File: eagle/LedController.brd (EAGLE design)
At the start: 64.8 x 34.3 mm, 21 parts, among them IC2 MEGA8-P, IC3 7805, Q1 16MHz, Q2 FDS8884, Q3 FDS8884, Q4 FDS8884, Q5 FDS8884, X1 2510-, X2 MKDSN1,5/4-5,08

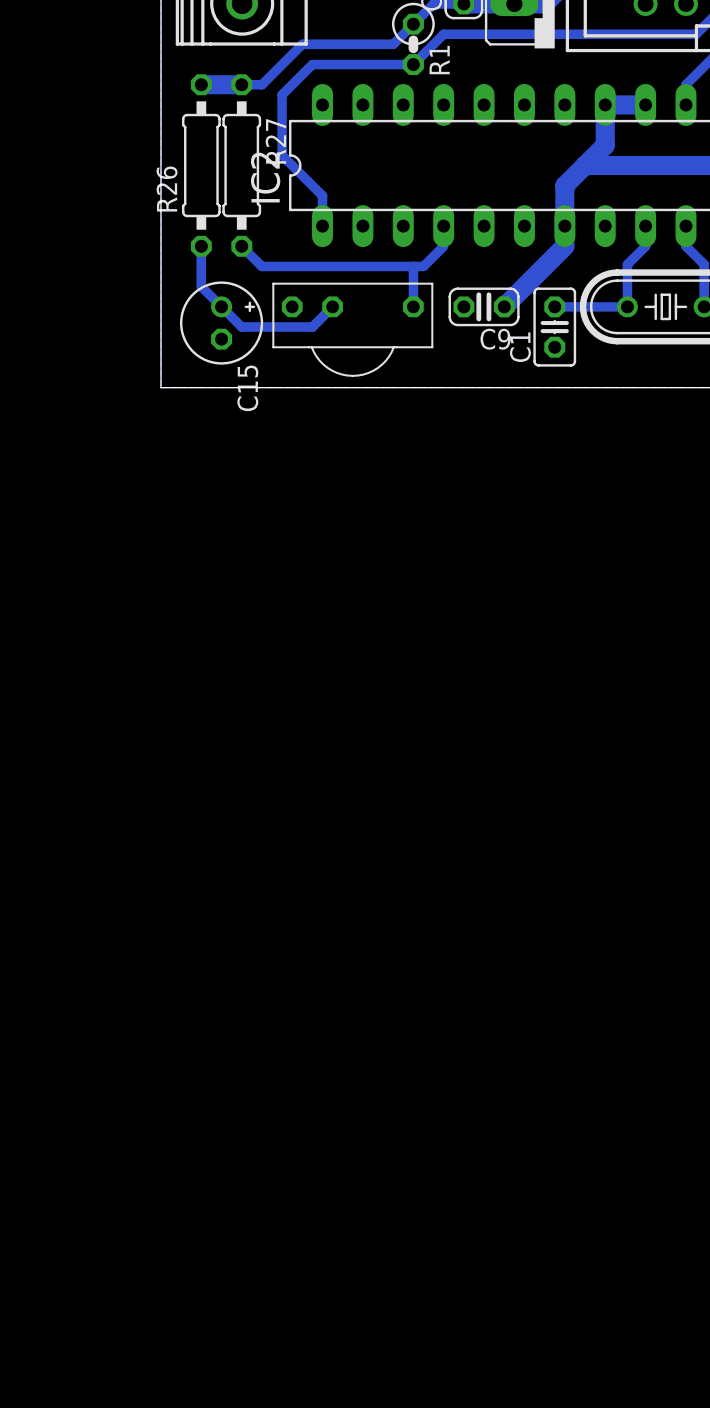
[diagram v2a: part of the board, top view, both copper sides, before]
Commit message: add preamp stage for microphone
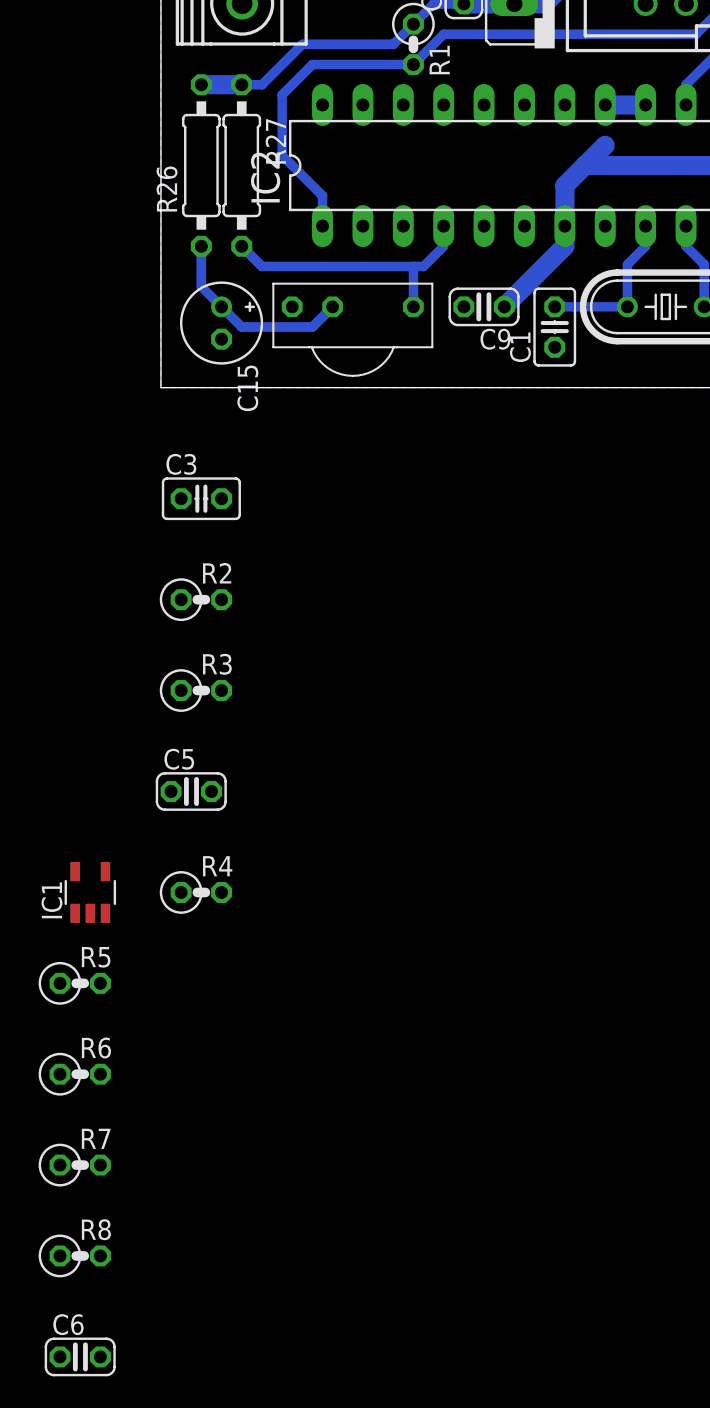
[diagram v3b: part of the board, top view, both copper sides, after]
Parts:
- added C3: 100nF, rcl:C025-025X050
- added C5: 1uF, rcl:C025-024X044
- added C6: 4n7, rcl:C025-024X044
- added IC1: MCP601R, linear:SOT23-5
- added R2: 100, rcl:0207/2V
- added R3, R4: 1k, rcl:0207/2V
- added R5, R6, R7: 10k, rcl:0207/2V
- added R8: 12k, rcl:0207/2V
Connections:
- new net ADC: C6.2, IC2.23, R8.2
- new net N$1: C5.1, R3.1
- new net N$10: IC1.4, R4.1
- new net N$11: IC1.3, R5.2, R6.1
- new net N$12: IC1.1, R7.2, R8.1
- new net N$7: C3.1, IC2.20, IC2.21, R2.1
- new net N$9: C5.2, R4.2, R7.1
- net +5V: now also IC1.2, R2.2, R3.2, R5.1; no longer IC2.20, IC2.21
- net GND: now also C3.2, C6.1, IC1.5, R6.2
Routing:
- net +5V: track 98.4 -> 93.3 mm
- net N$7: track 0.00 -> 2.54 mm
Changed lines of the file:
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@@
 <element name="R1" library="rcl" package="0207/2V" value="10k" x="15.875" y="21.59" rot="R270"/>
 <element name="Q5" library="FDS8884" package="SO08" value="FDS8884" x="12.065" y="28.575" rot="MR180"/>
+<element name="C3" library="rcl" package="C025-025X050" value="100nF" x="2.54" y="-6.985"/>
+<element name="R2" library="rcl" package="0207/2V" value="100" x="2.54" y="-13.335"/>
+<element name="R3" library="rcl" package="0207/2V" value="1k" x="2.54" y="-19.05"/>
+<element name="C5" library="rcl" package="C025-024X044" value="1uF" x="1.905" y="-25.4"/>
+<element name="R4" library="rcl" package="0207/2V" value="1k" x="2.54" y="-31.75"/>
+<element name="IC1" library="linear" package="SOT23-5" value="MCP601R" x="-4.445" y="-31.75"/>
+<element name="R5" library="rcl" package="0207/2V" value="10k" x="-5.08" y="-37.465"/>
+<element name="R6" library="rcl" package="0207/2V" value="10k" x="-5.08" y="-43.18"/>
+<element name="R7" library="rcl" package="0207/2V" value="10k" x="-5.08" y="-48.895"/>
+<element name="R8" library="rcl" package="0207/2V" value="12k" x="-5.08" y="-54.61"/>
+<element name="C6" library="rcl" package="C025-024X044" value="4n7" x="-5.08" y="-60.96"/>
 </elements>
 <signals>
@@
 <contactref element="Q5" pad="2"/>
 <contactref element="Q5" pad="3"/>
+<contactref element="C3" pad="2"/>
+<contactref element="R6" pad="2"/>
+<contactref element="IC1" pad="5"/>
+<contactref element="C6" pad="1"/>
+<wire x1="38.1" y1="26.67" x2="40.64" y2="26.67" width="0" layer="19" extent="1-1"/>
+<wire x1="35.56" y1="26.67" x2="38.1" y2="26.67" width="0" layer="19" extent="1-1"/>
+<wire x1="33.02" y1="26.67" x2="35.56" y2="26.67" width="0" layer="19" extent="1-1"/>
+<wire x1="22.225" y1="26.67" x2="33.02" y2="26.67" width="0" layer="19" extent="1-1"/>
+<wire x1="19.05" y1="26.67" x2="22.225" y2="26.67" width="0" layer="19" extent="1-1"/>
+<wire x1="16.51" y1="26.67" x2="19.05" y2="26.67" width="0" layer="19" extent="1-1"/>
+<wire x1="16.764" y1="31.75" x2="16.51" y2="26.67" width="0" layer="19" extent="1-1"/>
+<wire x1="12.7" y1="31.6484" x2="16.764" y2="31.75" width="0" layer="19" extent="16-16"/>
+<wire x1="11.43" y1="31.6484" x2="12.7" y2="31.6484" width="0" layer="19" extent="16-16"/>
+<wire x1="10.16" y1="31.6484" x2="11.43" y2="31.6484" width="0" layer="19" extent="16-16"/>
+<wire x1="25.4" y1="17.78" x2="22.225" y2="26.67" width="0" layer="19" extent="1-1"/>
+<wire x1="27.94" y1="10.16" x2="25.4" y2="17.78" width="0" layer="19" extent="1-1"/>
+<wire x1="24.765" y1="2.54" x2="27.94" y2="10.16" width="0" layer="19" extent="1-1"/>
+<wire x1="19.05" y1="5.08" x2="24.765" y2="2.54" width="0" layer="19" extent="1-1"/>
+<wire x1="8.255" y1="5.08" x2="19.05" y2="5.08" width="0" layer="19" extent="1-1"/>
+<wire x1="3.81" y1="3.048" x2="8.255" y2="5.08" width="0" layer="19" extent="1-1"/>
+<wire x1="3.81" y1="-6.985" x2="3.81" y2="3.048" width="0" layer="19" extent="1-1"/>
+<wire x1="38.735" y1="2.54" x2="27.94" y2="10.16" width="0" layer="19" extent="1-1"/>
+<wire x1="50.2666" y1="3.175" x2="38.735" y2="2.54" width="0" layer="19" extent="16-16"/>
+<wire x1="50.2666" y1="4.445" x2="50.2666" y2="3.175" width="0" layer="19" extent="16-16"/>
+<wire x1="50.2666" y1="1.905" x2="50.2666" y2="3.175" width="0" layer="19" extent="16-16"/>
+<wire x1="50.2666" y1="8.255" x2="50.2666" y2="4.445" width="0" layer="19" extent="16-16"/>
+<wire x1="50.2666" y1="9.525" x2="50.2666" y2="8.255" width="0" layer="19" extent="16-16"/>
+<wire x1="50.2666" y1="10.795" x2="50.2666" y2="9.525" width="0" layer="19" extent="16-16"/>
+<wire x1="50.2666" y1="14.605" x2="50.2666" y2="10.795" width="0" layer="19" extent="16-16"/>
+<wire x1="50.2666" y1="15.875" x2="50.2666" y2="14.605" width="0" layer="19" extent="16-16"/>
+<wire x1="50.2666" y1="17.145" x2="50.2666" y2="15.875" width="0" layer="19" extent="16-16"/>
+<wire x1="-5.395" y1="-30.444" x2="3.81" y2="-6.985" width="0" layer="19" extent="1-1"/>
+<wire x1="-3.81" y1="-43.18" x2="-5.395" y2="-30.444" width="0" layer="19" extent="1-1"/>
+<wire x1="-6.35" y1="-60.96" x2="-3.81" y2="-43.18" width="0" layer="19" extent="1-1"/>
 </signal>
 <signal name="N$2">
@@
 <contactref element="IC2" pad="7"/>
 <contactref element="R1" pad="1"/>
-<contactref element="IC2" pad="21"/>
-<contactref element="IC2" pad="20"/>
 <contactref element="R27" pad="1"/>
 <contactref element="R26" pad="2"/>
@@
 <wire x1="25.4" y1="12.7" x2="26.67" y2="13.97" width="1.2" layer="16"/>
 <wire x1="26.67" y1="13.97" x2="27.94" y2="15.24" width="1.2" layer="16"/>
-<wire x1="27.94" y1="15.24" x2="27.94" y2="17.78" width="1.2" layer="16"/>
 <wire x1="22.225" y1="24.13" x2="24.13" y2="24.13" width="1.2" layer="16"/>
 <wire x1="24.13" y1="24.13" x2="29.21" y2="29.21" width="1.2" layer="16"/>
@@
 <wire x1="43.18" y1="13.97" x2="26.67" y2="13.97" width="1.2" layer="16"/>
 <wire x1="30.48" y1="26.67" x2="30.48" y2="29.21" width="1.2" layer="16"/>
-<wire x1="27.94" y1="17.78" x2="30.48" y2="17.78" width="1.2" layer="16"/>
 <wire x1="2.54" y1="19.05" x2="5.08" y2="19.05" width="1.2" layer="16"/>
 <wire x1="19.05" y1="24.13" x2="22.225" y2="24.13" width="1.2" layer="16"/>
@@
 <wire x1="15.875" y1="22.86" x2="17.145" y2="24.13" width="0.6" layer="16"/>
 <wire x1="17.145" y1="24.13" x2="19.05" y2="24.13" width="0.6" layer="16"/>
+<contactref element="R2" pad="2"/>
+<contactref element="R3" pad="2"/>
+<contactref element="R5" pad="1"/>
+<contactref element="IC1" pad="2"/>
+<wire x1="-4.445" y1="-33.056" x2="-6.35" y2="-37.465" width="0" layer="19" extent="1-1"/>
+<wire x1="3.81" y1="-19.05" x2="-4.445" y2="-33.056" width="0" layer="19" extent="1-1"/>
+<wire x1="3.81" y1="-13.335" x2="3.81" y2="-19.05" width="0" layer="19" extent="1-1"/>
+<wire x1="21.59" y1="5.08" x2="3.81" y2="-13.335" width="0" layer="19" extent="1-1"/>
 </signal>
 <signal name="ISP_RESET">
@@
 <wire x1="38.1" y1="8.89" x2="38.1" y2="10.16" width="0.6" layer="16"/>
 </signal>
+<signal name="ADC">
+<contactref element="IC2" pad="23"/>
+<contactref element="R8" pad="2"/>
+<contactref element="C6" pad="2"/>
+<wire x1="-3.81" y1="-54.61" x2="-3.81" y2="-60.96" width="0" layer="19" extent="1-1"/>
+<wire x1="22.86" y1="17.78" x2="-3.81" y2="-54.61" width="0" layer="19" extent="1-1"/>
+</signal>
+<signal name="N$7">
+<contactref element="IC2" pad="21"/>
+<contactref element="IC2" pad="20"/>
+<wire x1="27.94" y1="17.78" x2="30.48" y2="17.78" width="1.2" layer="16"/>
+<contactref element="R2" pad="1"/>
+<contactref element="C3" pad="1"/>
+<wire x1="1.27" y1="-6.985" x2="27.94" y2="17.78" width="0" layer="19" extent="1-1"/>
+<wire x1="1.27" y1="-13.335" x2="1.27" y2="-6.985" width="0" layer="19" extent="1-1"/>
+</signal>
+<signal name="N$1">
+<contactref element="R3" pad="1"/>
+<contactref element="C5" pad="1"/>
+<wire x1="1.27" y1="-19.05" x2="0.635" y2="-25.4" width="0" layer="19" extent="1-1"/>
+</signal>
+<signal name="N$9">
+<contactref element="C5" pad="2"/>
+<contactref element="R4" pad="2"/>
+<contactref element="R7" pad="1"/>
+<wire x1="3.81" y1="-31.75" x2="-6.35" y2="-48.895" width="0" layer="19" extent="1-1"/>
+<wire x1="3.175" y1="-25.4" x2="3.81" y2="-31.75" width="0" layer="19" extent="1-1"/>
+</signal>
+<signal name="N$10">
+<contactref element="R4" pad="1"/>
+<contactref element="IC1" pad="4"/>
+<wire x1="-3.495" y1="-30.444" x2="1.27" y2="-31.75" width="0" layer="19" extent="1-1"/>
+</signal>
+<signal name="N$11">
+<contactref element="R5" pad="2"/>
+<contactref element="R6" pad="1"/>
+<contactref element="IC1" pad="3"/>
+<wire x1="-3.81" y1="-37.465" x2="-6.35" y2="-43.18" width="0" layer="19" extent="1-1"/>
+<wire x1="-3.495" y1="-33.056" x2="-3.81" y2="-37.465" width="0" layer="19" extent="1-1"/>
+</signal>
+<signal name="N$12">
+<contactref element="R7" pad="2"/>
+<contactref element="IC1" pad="1"/>
+<contactref element="R8" pad="1"/>
+<wire x1="-3.81" y1="-48.895" x2="-6.35" y2="-54.61" width="0" layer="19" extent="1-1"/>
+<wire x1="-5.395" y1="-33.056" x2="-3.81" y2="-48.895" width="0" layer="19" extent="1-1"/>
+</signal>
 </signals>

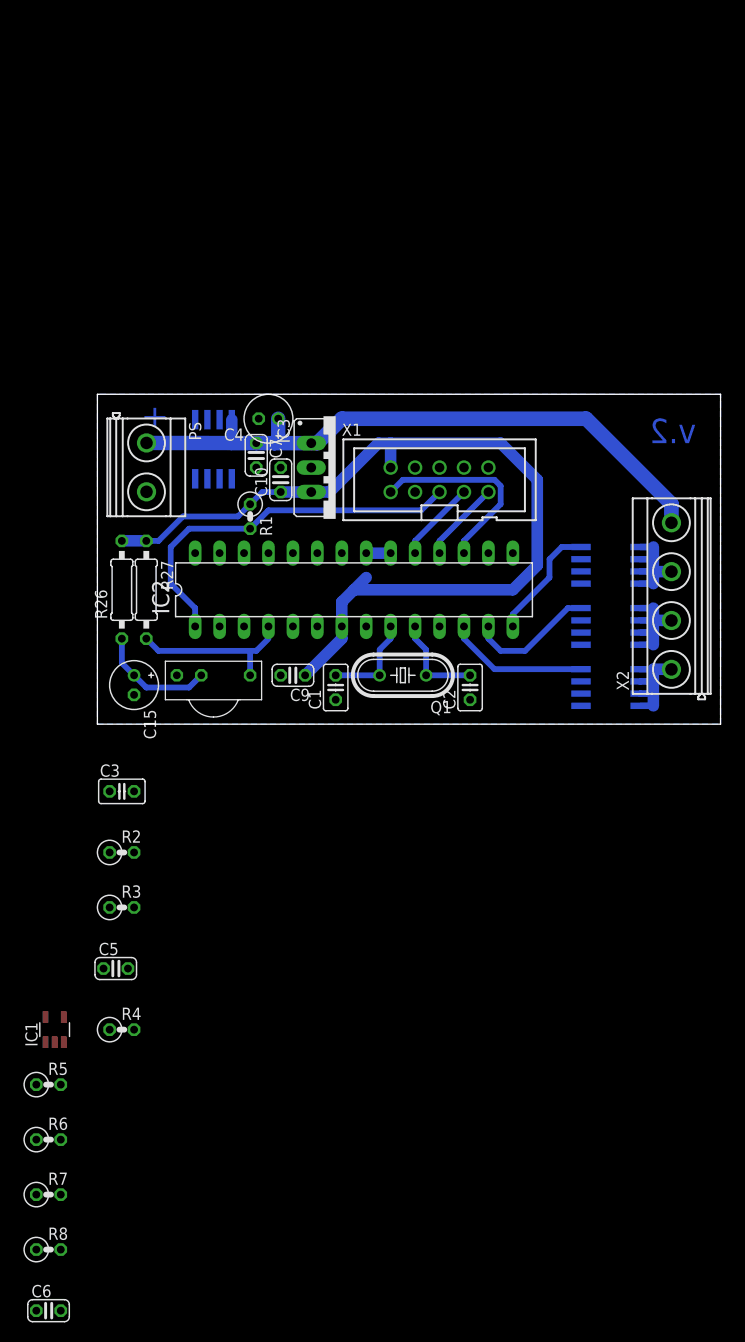
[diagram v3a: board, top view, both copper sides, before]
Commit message: Replace atmega8 (DIP) with atmega328 (TQFP), start of redesign
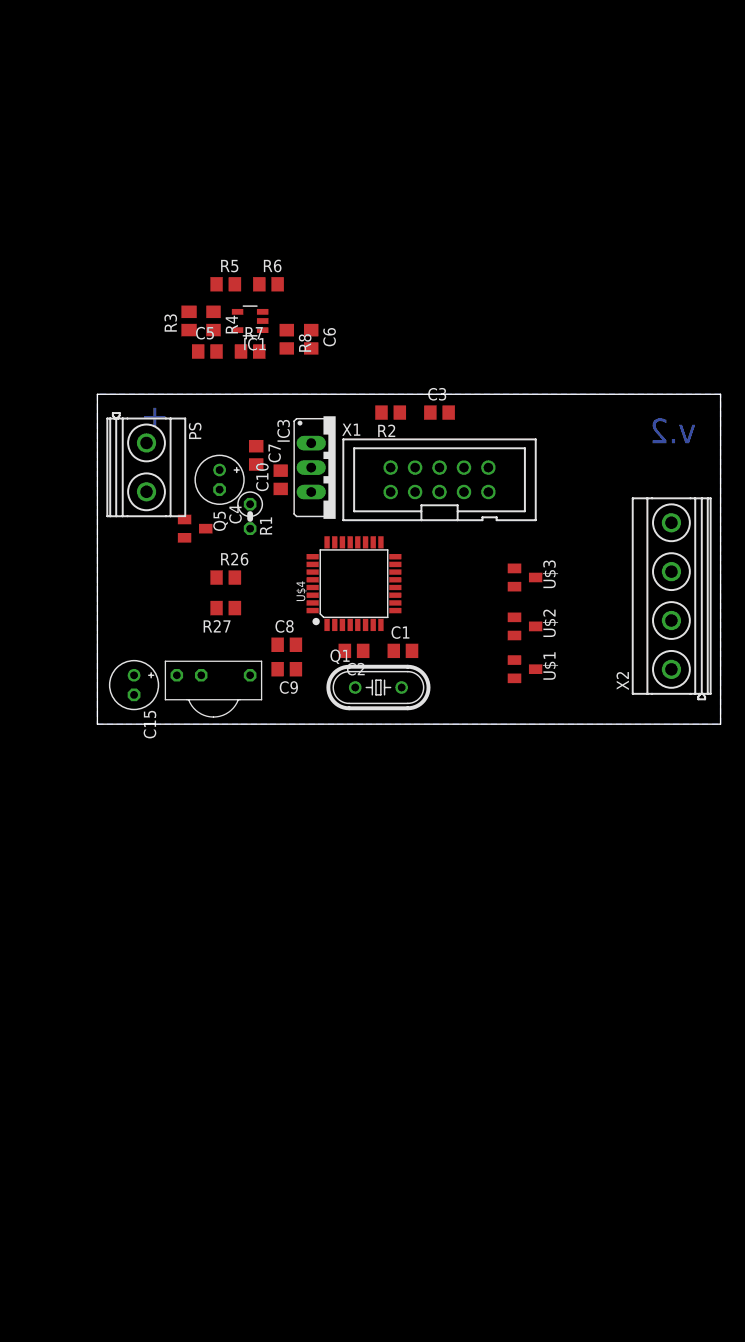
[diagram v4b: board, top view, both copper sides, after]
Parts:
- removed IC2: MEGA8-P, atmel:DIL28-3
- removed Q2, Q3, Q4: FDS8884, FDS8884:SO08
- added C8: 100nF, rcl:C0805
- added U$1, U$2, U$3: PMV20EN, LedController:SOT23
- added U$4: ATMEGA328, LedController:TQFP32
- C1, C2, C3: device rcl:C025-025X050 -> rcl:C0805
- C10, C5, C6, C7, C9: device rcl:C025-024X044 -> rcl:C0805
- Q5: value FDS8884 -> PMV20EN; device FDS8884:SO08 -> LedController:SOT23
- R2, R4, R5, R6, R7, R8: device rcl:0207/2V -> rcl:R0805
- R26, R27: device rcl:0207/10 -> rcl:R0805
- R3: device rcl:0207/2V -> rcl:M0805
- moved C6 104.6 mm to (22.2, 40.0), turned to 270 degrees
- moved R8 97.8 mm to (19.7, 40.0), turned to 270 degrees
- moved R6 91.8 mm to (17.8, 45.7)
- moved R7 90.1 mm to (15.9, 38.7)
- moved R5 85.2 mm to (13.3, 45.7)
- moved IC1 76.4 mm to (15.9, 41.9), turned to 90 degrees
- moved R4 74.3 mm to (12.1, 41.9), turned to 270 degrees
- moved C5 64.8 mm to (11.4, 38.7)
- moved R3 61.4 mm to (9.53, 41.9), turned to 90 degrees
- moved R2 53.6 mm to (30.5, 32.4), turned to 180 degrees
- moved C3 51.4 mm to (35.6, 32.4)
- moved C2 12.7 mm to (26.7, 7.62), turned to 180 degrees
- moved R26 10.9 mm to (13.3, 15.2), turned to 0 degrees
- moved R27 8.47 mm to (13.3, 12.1), turned to 180 degrees
- moved Q5 8.47 mm to (10.2, 20.3), flipped to the top, turned to 270 degrees
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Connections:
- removed net N$2: C1.2, IC2.9, Q1.2
- new net N$13: C1.2, Q1.2, U$4.8
- net +12V: now also Q5.1; no longer Q5.4
- net +5V: now also U$4.4, U$4.6; no longer C9.1, IC2.7
- net ADC: now also U$4.23; no longer IC2.23
- net GND: now also U$1.2, U$2.2, U$3.2, U$4.21, U$4.3, U$4.5; no longer C9.2, IC2.22, IC2.8, Q2.1, Q2.2, Q2.3, Q3.1, Q3.2, Q3.3, Q4.1, Q4.2, Q4.3, Q5.1, Q5.3
- net IR: now also U$4.32; no longer IC2.4
- net ISP_CLK: now also U$4.17; no longer IC2.19
- net ISP_MISO: now also U$4.16; no longer IC2.18
- net ISP_MOSI: now also U$4.15; no longer IC2.17
- net ISP_RESET: now also U$4.29; no longer IC2.1
- net N$3: now also U$4.7; no longer IC2.10
- net N$4: now also U$1.3; no longer Q2.5, Q2.6, Q2.7, Q2.8
- net N$5: now also U$2.3; no longer Q3.5, Q3.6, Q3.7, Q3.8
- net N$6: now also U$3.3; no longer Q4.5, Q4.6, Q4.7, Q4.8
- net N$7: now also U$4.18, U$4.20; no longer IC2.20, IC2.21
- net N$8: now also Q5.3; no longer Q5.5, Q5.6, Q5.7, Q5.8
- net PWM_B: now also U$3.1, U$4.12; no longer IC2.14, Q4.4
- net PWM_G: now also U$2.1, U$4.11; no longer IC2.13, Q3.4
- net PWM_R: now also U$1.1, U$4.10; no longer IC2.12, Q2.4
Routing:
- net +5V: track 93.3 -> 0.00 mm
- net +12V: track 66.4 -> 0.00 mm
- net ISP_RESET: track 39.6 -> 0.00 mm
- net ISP_MOSI: track 20.8 -> 0.00 mm
- net IR: track 16.3 -> 0.00 mm
- net PWM_R: track 14.8 -> 0.00 mm
- net PWM_G: track 13.3 -> 0.00 mm
- net N$63: track 12.4 -> 0.00 mm
- net PWM_B: track 12.4 -> 0.00 mm
- net N$5: track 11.6 -> 0.00 mm
- net N$6: track 11.4 -> 0.00 mm
- net N$4: track 11.2 -> 0.00 mm
- net N$2: track 10.1 -> 0.00 mm
- net N$3: track 10.1 -> 0.00 mm
- net ISP_MISO: track 8.45 -> 0.00 mm
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
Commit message: Change IR Receiver module to SMD variant
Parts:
- removed R27: 10k, rcl:R0805
- removed TSOP: TSOP, TSOP1736:TSOP
- added U$5: TSOP75236, LedController:TSOP75236
- R1: device rcl:0207/2V -> rcl:R0805
- moved C15 11.1 mm to (14.9, 3.81), turned to 180 degrees
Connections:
- net +5V: no longer R27.1
- net GND: now also U$5.P$1, U$5.P$4; no longer TSOP.GND
- net IR: now also U$5.P$3; no longer R27.2, TSOP.VO
- net N$63: now also U$5.P$2; no longer TSOP.VS
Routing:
- added copper zone on layer 1, net GND
- removed copper zone on layer 16, net GND
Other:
- board text removed: "+"
- board text removed: "v.2"
